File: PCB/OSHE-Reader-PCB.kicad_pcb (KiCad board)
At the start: 2 copper layers, 5 parts, among them J2 112L-TDA0, U1 BQ2057CSNTR, U2 IRF7326D2TRPBF, U3 TPS5432DDA

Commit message: misc work on schematic
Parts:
- added J1: USB_C_Receptacle_PowerOnly_24P, USB4125_GF_A:CONN6_USB4125_GCT, F.Cu at (79.5, 26.7)
- added J3: Conn_01x24_MountingPin, FH12A_24S_0_5SH_55_:CONN24_1X24_DRC_FFC_HIR, F.Cu at (63.6, 45.4)
- added R_{SNS}1: 0.1, WSL2512R1000FEA:RES_2512_WSL, F.Cu at (58.7, 54.8)
- added R_{SNS}2: 0.1, WSL2512R1000FEA:RES_2512_WSL, F.Cu at (58.7, 59.9)
- added U4: ~, ESP32-C6-DEV-KIT-N8:ESP32-C6-DEV-KIT-N8, F.Cu at (38.1, 48.7)
- moved CR1 50.9 mm to (75.5, 32.5)
- moved J2 32.3 mm to (62.3, 31.0)
- moved U3 18.1 mm to (78.0, 55.6)
- moved U1 13.9 mm to (58.5, 65.8)
- moved U2 5.55 mm to (67.4, 55.6)
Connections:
- J2 pad 19: unconnected-(J2-GND-Pad19) -> /SD Card/GND
- J2 pad 2: unconnected-(J2-CD/DAT3-Pad2) -> /SD Card/CS
- J2 pad 20: unconnected-(J2-GND-Pad20) -> /SD Card/GND
- J2 pad 21: unconnected-(J2-GND-Pad21) -> /SD Card/GND
- J2 pad 22: unconnected-(J2-GND-Pad22) -> /SD Card/GND
- J2 pad 23: unconnected-(J2-GND-Pad23) -> /SD Card/GND
- J2 pad 4: unconnected-(J2-VDD-Pad4) -> /SD Card/3V3
- J2 pad 6: unconnected-(J2-VSS-Pad6) -> /SD Card/GND
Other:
- board outline added: 8.7 x 4.4 mm

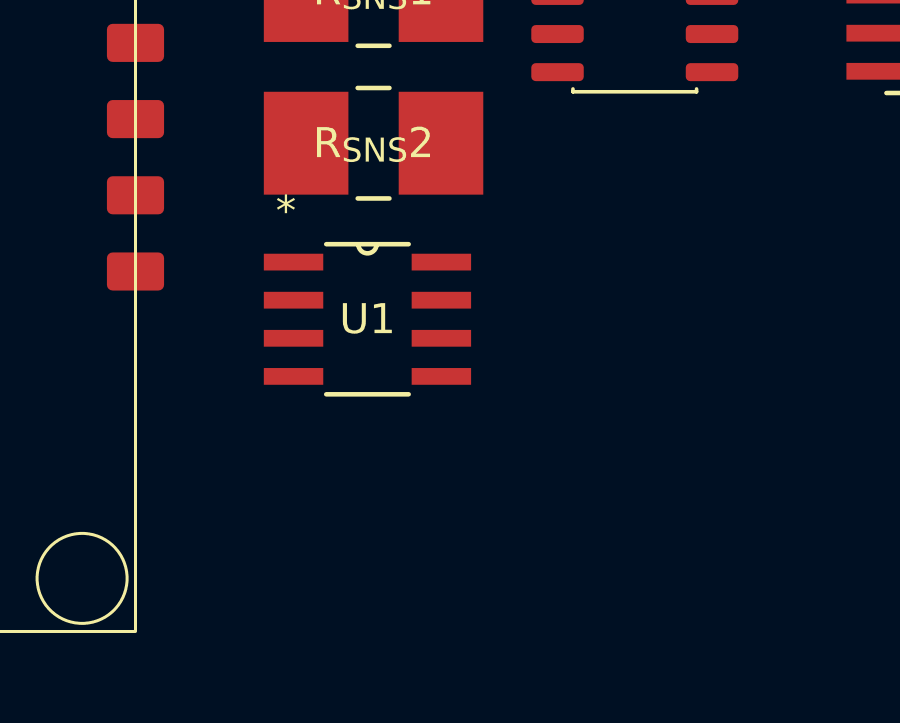
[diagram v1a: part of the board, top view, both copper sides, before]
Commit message: put 3v3 on high side of buttons instead of hierarchical pins
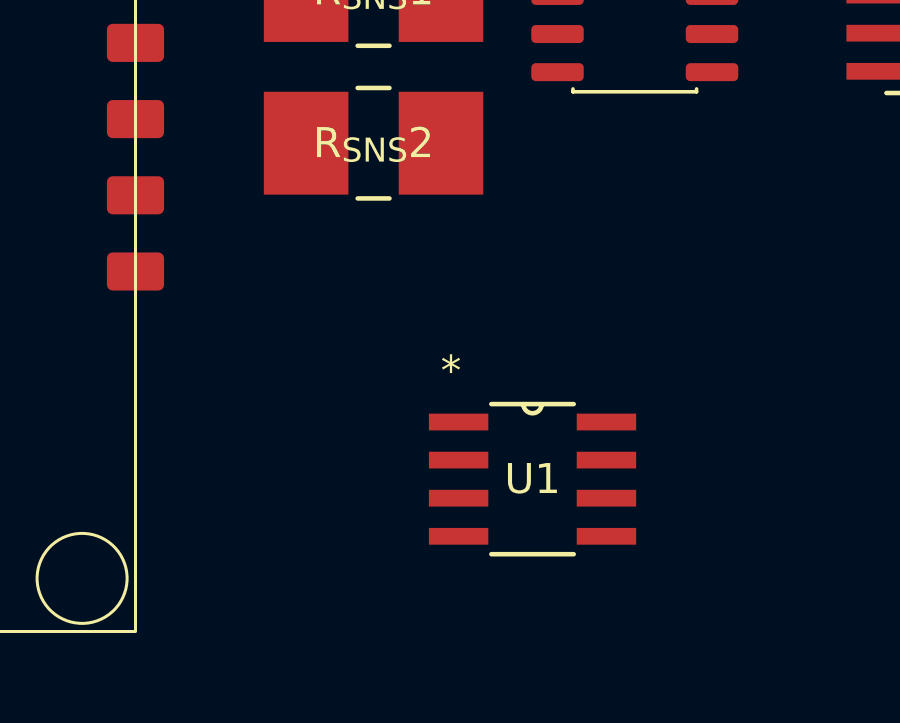
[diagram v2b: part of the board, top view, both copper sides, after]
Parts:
- R_{SNS}1, R_{SNS}2: value 0.1 -> 0.2
- moved U1 7.66 mm to (64.0, 71.1)
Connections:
- U1 pad 1: /Battery Charging/VBUS -> Net-(Q1-E)
- U1 pad 2: /Battery Charging/TS -> /Battery Charging/BAT+
- U1 pad 3: /BAT_STAT -> /Battery Charging/VBUS
- U1 pad 4: GND -> /Battery Charging/TS
- U1 pad 5: Net-(U1-CC) -> /BAT_STAT
- U1 pad 6: /Battery Charging/VBUS -> GND
- U1 pad 7: Net-(Q1-E) -> Net-(U1-CC)
- U1 pad 8: /Battery Charging/BAT+ -> /Battery Charging/VBUS

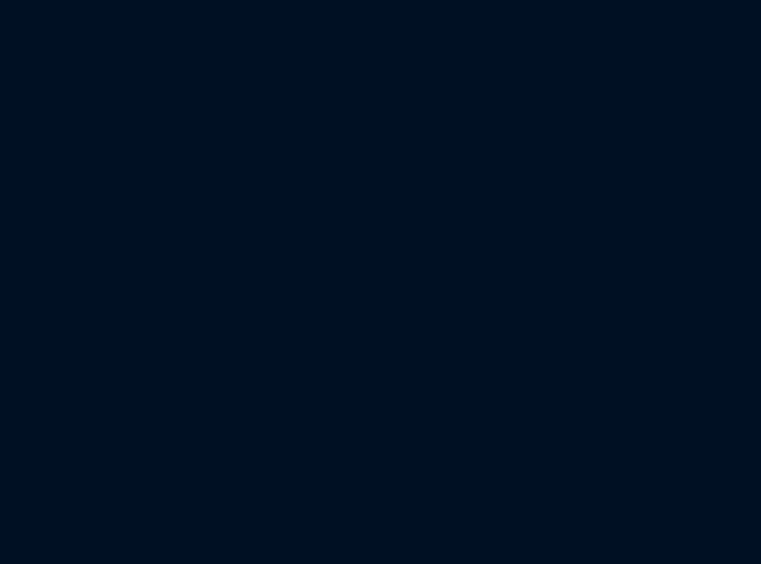
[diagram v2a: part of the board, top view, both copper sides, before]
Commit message: added fuses to schematic, updated pcb with new components
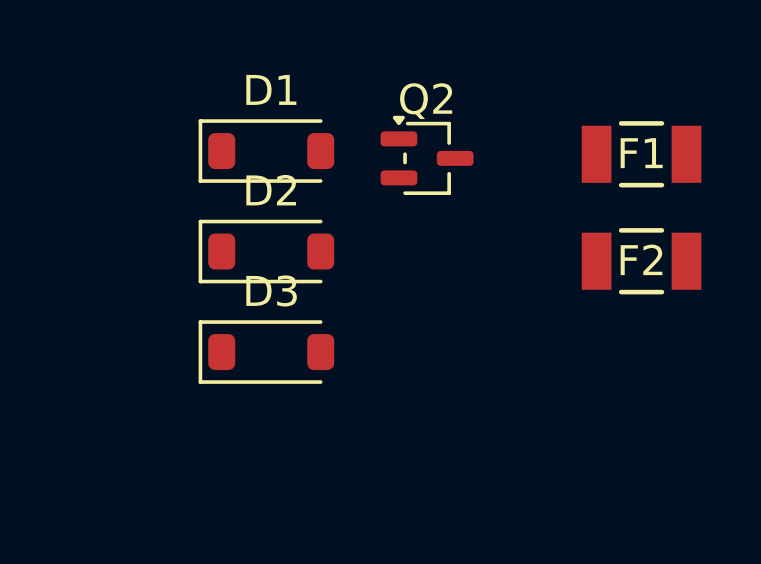
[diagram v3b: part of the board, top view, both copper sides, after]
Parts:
- added D1: MBR0530, Diode_SMD:D_SOD-123, F.Cu at (100.9, 23.7)
- added D2: MBR0530, Diode_SMD:D_SOD-123, F.Cu at (100.9, 27.0)
- added D3: MBR0530, Diode_SMD:D_SOD-123, F.Cu at (100.9, 30.4)
- added F1: 0ZCJ0050FF2G, 0ZCJ0050FF2G:0ZCJ_BEL, F.Cu at (113.3, 23.8)
- added F2: 0ZCJ0050FF2G, 0ZCJ0050FF2G:0ZCJ_BEL, F.Cu at (113.3, 27.3)
- added Q2: Si1308EDL, Package_TO_SOT_SMD:SOT-323_SC-70, F.Cu at (106.1, 23.9)
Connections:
- CR1 pad 1: /Battery Charging/VBUS -> /USB-C-Connector/VBUS
- J1 pad A9: /Battery Charging/VBUS -> /USB-C-Connector/VBUS
- J1 pad B9: /Battery Charging/VBUS -> /USB-C-Connector/VBUS
- J2 pad 19: /SD Card/GND -> GND
- J2 pad 2: /SD Card/CS -> /SD_CS
- J2 pad 20: /SD Card/GND -> GND
- J2 pad 21: /SD Card/GND -> GND
- J2 pad 22: /SD Card/GND -> GND
- J2 pad 23: /SD Card/GND -> GND
- J2 pad 3: unconnected-(J2-CMD-Pad3) -> /COPI
- J2 pad 4: /SD Card/3V3 -> +3V3
- J2 pad 5: unconnected-(J2-CLK-Pad5) -> /SCK
- J2 pad 6: /SD Card/GND -> GND
- J2 pad 7: unconnected-(J2-DAT0-Pad7) -> /CIPO
- J3 pad 10: unconnected-(J3-RST_N-Pad10) -> /EP_RESET
- J3 pad 11: unconnected-(J3-DC-Pad11) -> /EP_D/C
- J3 pad 12: unconnected-(J3-CSB-Pad12) -> /EP_CS
- J3 pad 13: unconnected-(J3-SCLK-Pad13) -> /SCK
- J3 pad 14: unconnected-(J3-SDI-Pad14) -> /COPI
- J3 pad 15: unconnected-(J3-VDDIO-Pad15) -> +3V3
- J3 pad 16: unconnected-(J3-VDD-Pad16) -> +3V3
- J3 pad 17: unconnected-(J3-VSS-Pad17) -> GND
- J3 pad 18: unconnected-(J3-VDD_1V8-Pad18) -> Net-(J3-VDD_1V8)
- J3 pad 2: unconnected-(J3-GDR-Pad2) -> /Display Connector/GDR
- J3 pad 20: unconnected-(J3-VSH-Pad20) -> Net-(J3-VSH)
- J3 pad 21: unconnected-(J3-VGH-Pad21) -> /Display Connector/PREVGH
- J3 pad 22: unconnected-(J3-VSL-Pad22) -> Net-(J3-VSL)
- J3 pad 23: unconnected-(J3-VGL-Pad23) -> /Display Connector/PREVGL
- J3 pad 24: unconnected-(J3-VCOM-Pad24) -> Net-(J3-VCOM)
- J3 pad 3: unconnected-(J3-RESE-Pad3) -> /Display Connector/RESE
- J3 pad 5: unconnected-(J3-VSHR-Pad5) -> Net-(J3-VSHR)
- J3 pad 8: unconnected-(J3-BS-Pad8) -> GND
- J3 pad 9: unconnected-(J3-BUSY_N-Pad9) -> /EP_BUSY
- U3 pad 2: /Battery Charging/VOUT -> /Buck Converter/VIN
- U4 pad 1: /Microcontroller/3V3 -> +3V3
- U4 pad 10: unconnected-(U4-GPIO10-Pad10) -> /Buttons/UpButton
- U4 pad 11: unconnected-(U4-GPIO11-Pad11) -> /Buttons/DownButton
- U4 pad 12: unconnected-(U4-GPIO2-Pad12) -> /CIPO
- U4 pad 13: unconnected-(U4-GPIO3-Pad13) -> /EP_RESET
- U4 pad 15: /Microcontroller/GND -> GND
- U4 pad 17: /Microcontroller/GND -> GND
- U4 pad 21: unconnected-(U4-GPIO23-Pad21) -> /Buttons/LeftButton
- U4 pad 22: unconnected-(U4-GPIO22-Pad22) -> /Buttons/HomeButton
- U4 pad 23: unconnected-(U4-GPIO21-Pad23) -> /Buttons/RightButton
- U4 pad 24: unconnected-(U4-GPIO20-Pad24) -> /EP_D/C
- U4 pad 25: unconnected-(U4-GPIO19-Pad25) -> /EP_CS
- U4 pad 26: unconnected-(U4-GPIO18-Pad26) -> /SD_CS
- U4 pad 28: /Microcontroller/GND -> GND
- U4 pad 31: /Microcontroller/GND -> GND
- U4 pad 5: unconnected-(U4-GPIO6-Pad5) -> /SCK
- U4 pad 6: unconnected-(U4-GPIO7-Pad6) -> /COPI
- U4 pad 7: unconnected-(U4-GPIO0-Pad7) -> Net-(U4-GPIO0)
- U4 pad 8: unconnected-(U4-GPIO1-Pad8) -> /BAT_STAT
- U4 pad 9: unconnected-(U4-GPIO8-Pad9) -> /EP_BUSY

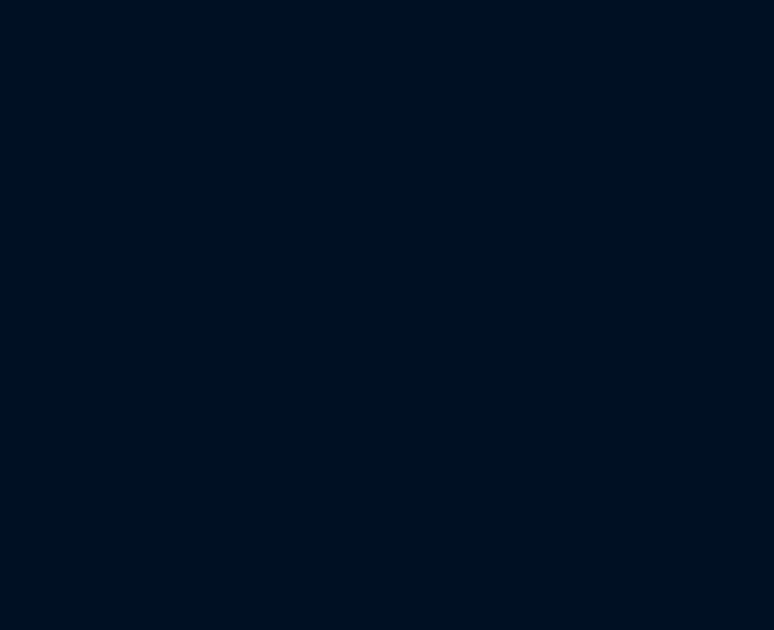
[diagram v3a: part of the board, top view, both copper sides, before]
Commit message: Update OSHE-Reader-PCB.kicad_pcb
Added resistor footprint
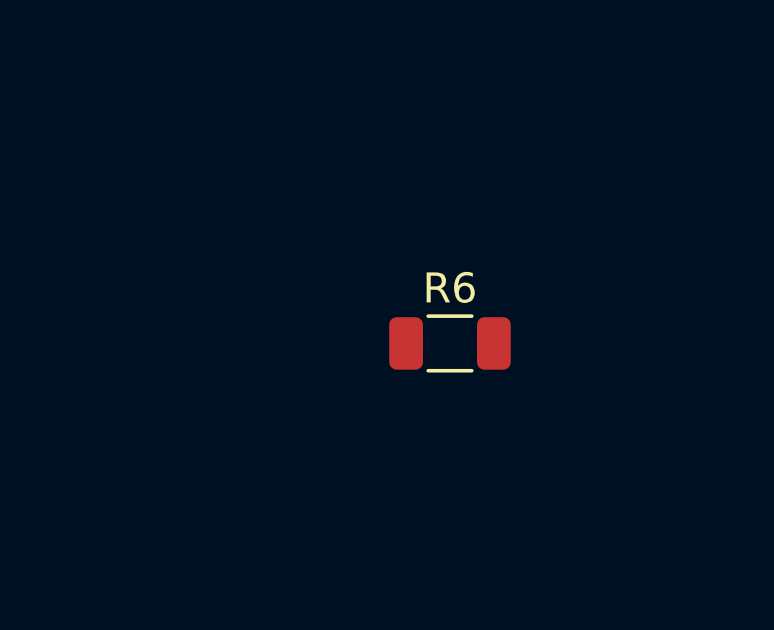
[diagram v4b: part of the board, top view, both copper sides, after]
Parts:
- added R6: 100K, Resistor_SMD:R_1206_3216Metric, F.Cu at (106.5, 61.0)
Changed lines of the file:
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@@
 	(net 75 "unconnected-(U4-UART_TXD-Pad18)")
 	(net 76 "unconnected-(U4-USB_N-Pad30)")
+	(footprint "Resistor_SMD:R_1206_3216Metric"
+		(layer "F.Cu")
+		(at 106.4625 61)
+		(descr "Resistor SMD 1206 (3216 Metric), square (rectangular) end terminal, IPC-7351 nominal, (Body size source: IPC-SM-782 page 72, https://www.pcb-3d.com/wordpress/wp-content/uploads/ipc-sm-782a_amendment_1_and_2.pdf), generated with kicad-footprint-generator")
+		(tags "resistor")
+		(property "Reference" "R6"
+			(at 0 -1.83 0)
+			(layer "F.SilkS")
+			(effects
+				(font
+					(size 1 1)
+					(thickness 0.15)
+				)
+			)
+		)
+		(property "Value" "100K"
+			(at 0 1.83 0)
+			(layer "F.Fab")
+			(effects
+				(font
+					(size 1 1)
+					(thickness 0.15)
+				)
+			)
+		)
+		(property "Datasheet" "~"
+			(at 0 0 0)
+			(layer "F.Fab")
+			(hide yes)
+			(effects
+				(font
+					(size 1.27 1.27)
+					(thickness 0.15)
+				)
+			)
+		)
+		(property "Description" "Resistor"
+			(at 0 0 0)
+			(layer "F.Fab")
+			(hide yes)
+			(effects
+				(font
+					(size 1.27 1.27)
+					(thickness 0.15)
+				)
+			)
+		)
+		(property ki_fp_filters "R_*")
+		(sheetname "/Battery Charging/")
+		(sheetfile "OSHE-Reader-Battery.kicad_sch")
+		(attr smd)
+		(fp_line
+			(start -0.727064 -0.91)
+			(end 0.727064 -0.91)
+			(stroke
+				(width 0.12)
+				(type solid)
+			)
+			(layer "F.SilkS")
+		)
+		(fp_line
+			(start -0.727064 0.91)
+			(end 0.727064 0.91)
+			(stroke
+				(width 0.12)
+				(type solid)
+			)
+			(layer "F.SilkS")
+		)
+		(fp_rect
+			(start -2.28 -1.13)
+			(end 2.28 1.13)
+			(stroke
+				(width 0.05)
+				(type solid)
+			)
+			(fill no)
+			(layer "F.CrtYd")
+		)
+		(fp_rect
+			(start -1.6 -0.8)
+			(end 1.6 0.8)
+			(stroke
+				(width 0.1)
+				(type solid)
+			)
+			(fill no)
+			(layer "F.Fab")
+		)
+		(fp_text user "${REFERENCE}"
+			(at 0 0 0)
+			(layer "F.Fab")
+			(effects
+				(font
+					(size 0.8 0.8)
+					(thickness 0.12)
+				)
+			)
+		)
+		(pad "1" smd roundrect
+			(at -1.4625 0)
+			(size 1.125 1.75)
+			(layers "F.Cu" "F.Mask" "F.Paste")
+			(roundrect_rratio 0.222222)
+			(net 1 "/Battery Charging/VBUS")
+			(pintype "passive")
+		)
+		(pad "2" smd roundrect
+			(at 1.4625 0)
+			(size 1.125 1.75)
+			(layers "F.Cu" "F.Mask" "F.Paste")
+			(roundrect_rratio 0.222222)
+			(net 2 "GND")
+			(pintype "passive")
+		)
+		(embedded_fonts no)
+		(model "${KICAD9_3DMODEL_DIR}/Resistor_SMD.3dshapes/R_1206_3216Metric.step"
+			(offset
+				(xyz 0 0 0)
+			)
+			(scale
+				(xyz 1 1 1)
+			)
+			(rotate
+				(xyz 0 0 0)
+			)
+		)
+	)
 	(footprint "FH12A_24S_0_5SH_55_:CONN24_1X24_DRC_FFC_HIR"
 		(layer "F.Cu")

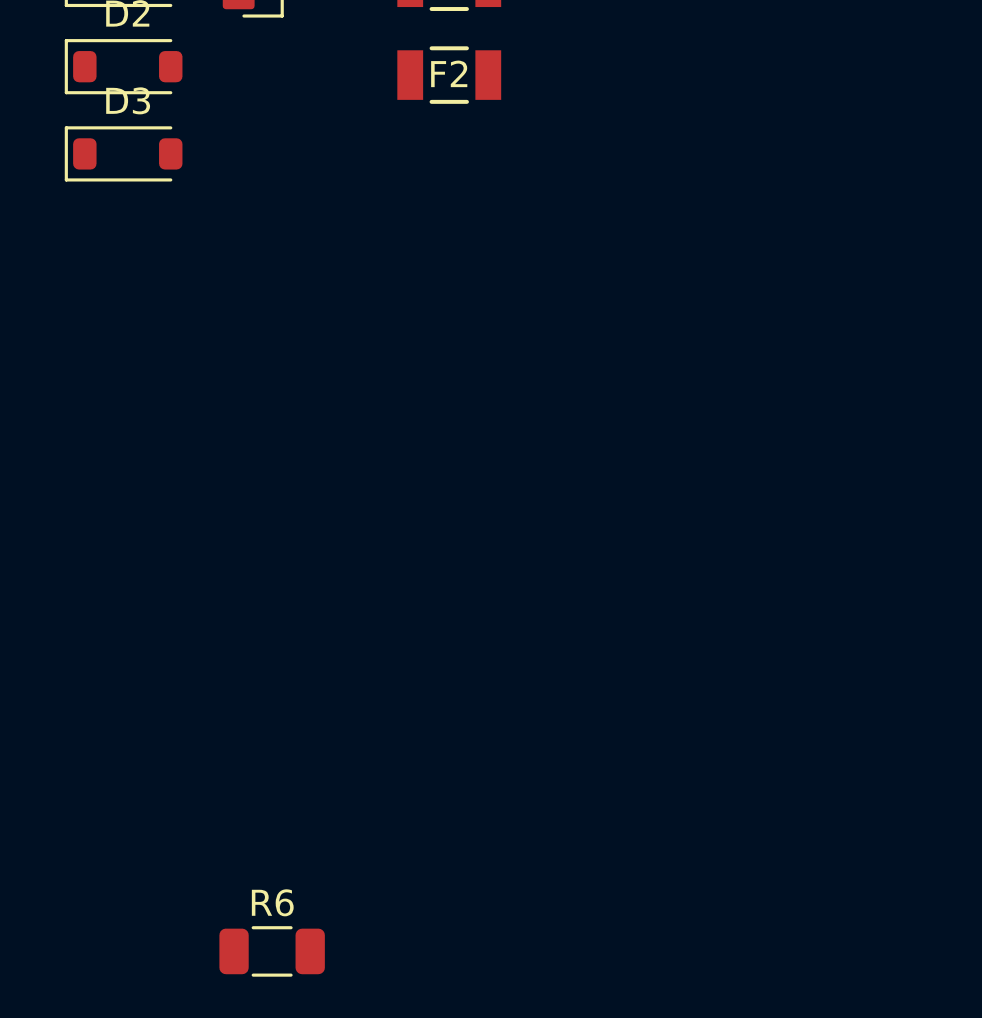
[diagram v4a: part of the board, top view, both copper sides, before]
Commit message: Footprint assignments
Added more footprints
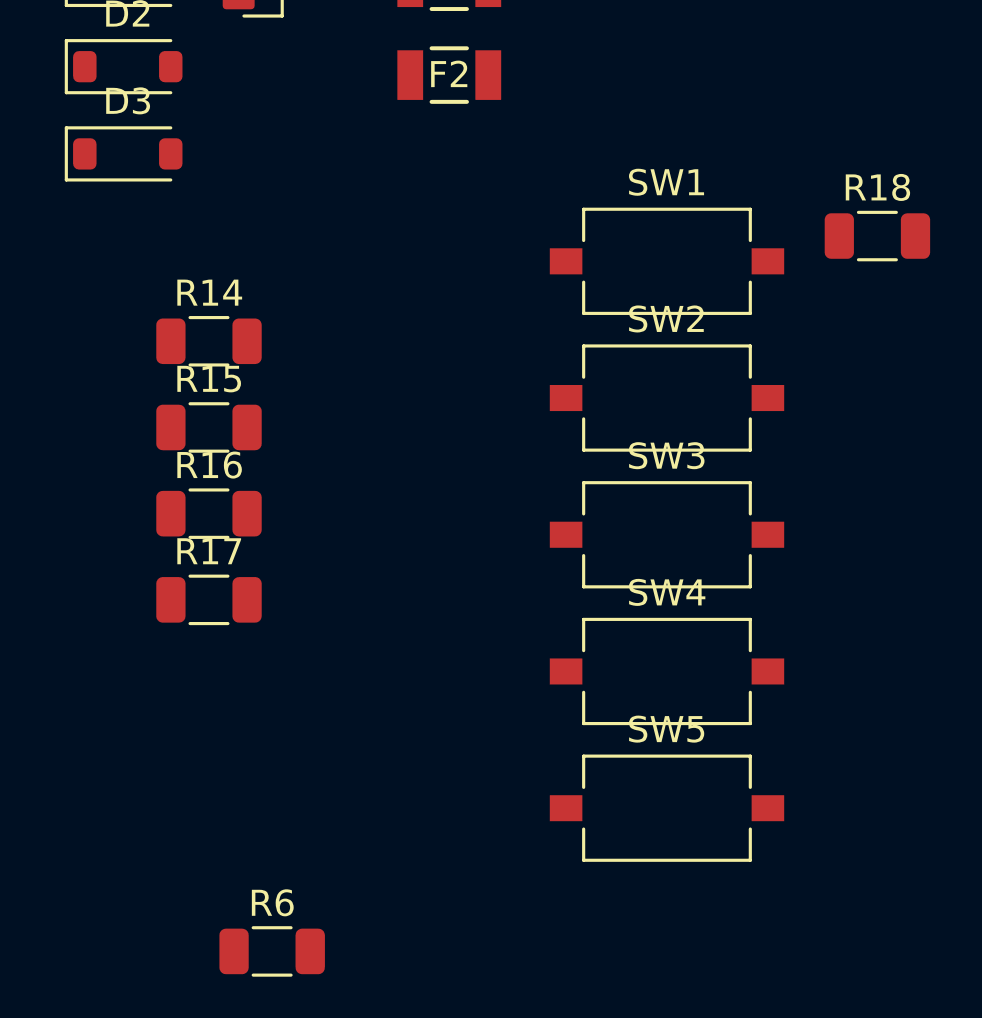
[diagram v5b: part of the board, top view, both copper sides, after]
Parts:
- added R14: 100k, Resistor_SMD:R_1206_3216Metric, F.Cu at (104.0, 37.6)
- added R15: 100k, Resistor_SMD:R_1206_3216Metric, F.Cu at (104.0, 40.9)
- added R16: 100k, Resistor_SMD:R_1206_3216Metric, F.Cu at (104.0, 44.2)
- added R17: 100k, Resistor_SMD:R_1206_3216Metric, F.Cu at (104.0, 47.5)
- added R18: 100k, Resistor_SMD:R_1206_3216Metric, F.Cu at (129.7, 33.5)
- added SW1: SW_Push, Button_Switch_SMD:SW_Tactile_SPST_NO_Straight_CK_PTS636Sx25SMTRLFS, F.Cu at (121.6, 34.5)
- added SW2: SW_Push, Button_Switch_SMD:SW_Tactile_SPST_NO_Straight_CK_PTS636Sx25SMTRLFS, F.Cu at (121.6, 39.8)
- added SW3: SW_Push, Button_Switch_SMD:SW_Tactile_SPST_NO_Straight_CK_PTS636Sx25SMTRLFS, F.Cu at (121.6, 45.0)
- added SW4: SW_Push, Button_Switch_SMD:SW_Tactile_SPST_NO_Straight_CK_PTS636Sx25SMTRLFS, F.Cu at (121.6, 50.2)
- added SW5: SW_Push, Button_Switch_SMD:SW_Tactile_SPST_NO_Straight_CK_PTS636Sx25SMTRLFS, F.Cu at (121.6, 55.5)
